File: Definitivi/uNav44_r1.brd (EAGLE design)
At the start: 39.6 x 39.6 mm, 37 parts, among them IC1 DSPIC33FJ128MC, IC2 24LC024, Q1 10MHz

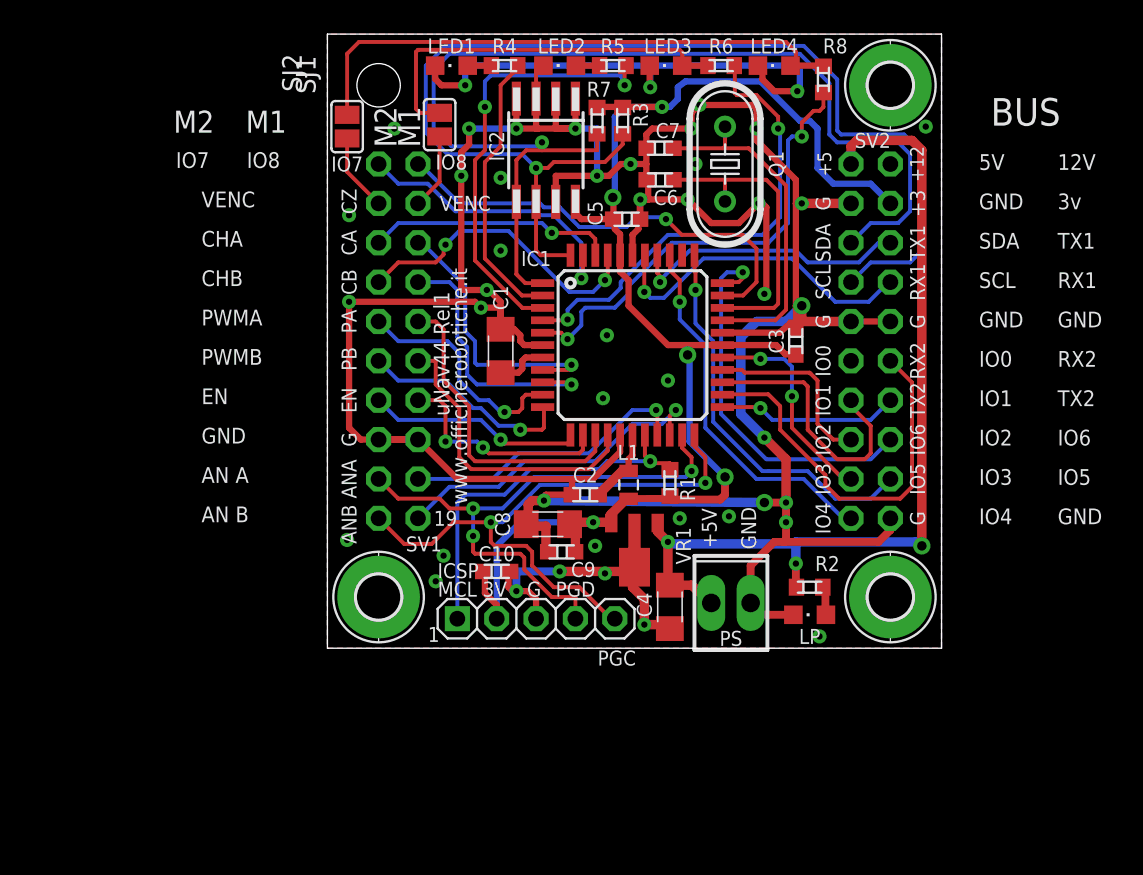
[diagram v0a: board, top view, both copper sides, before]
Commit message: Add Vencoder voltage selection \ Removed connection of LED3 and LED4 from connector \ @katodo : PCB update is needed
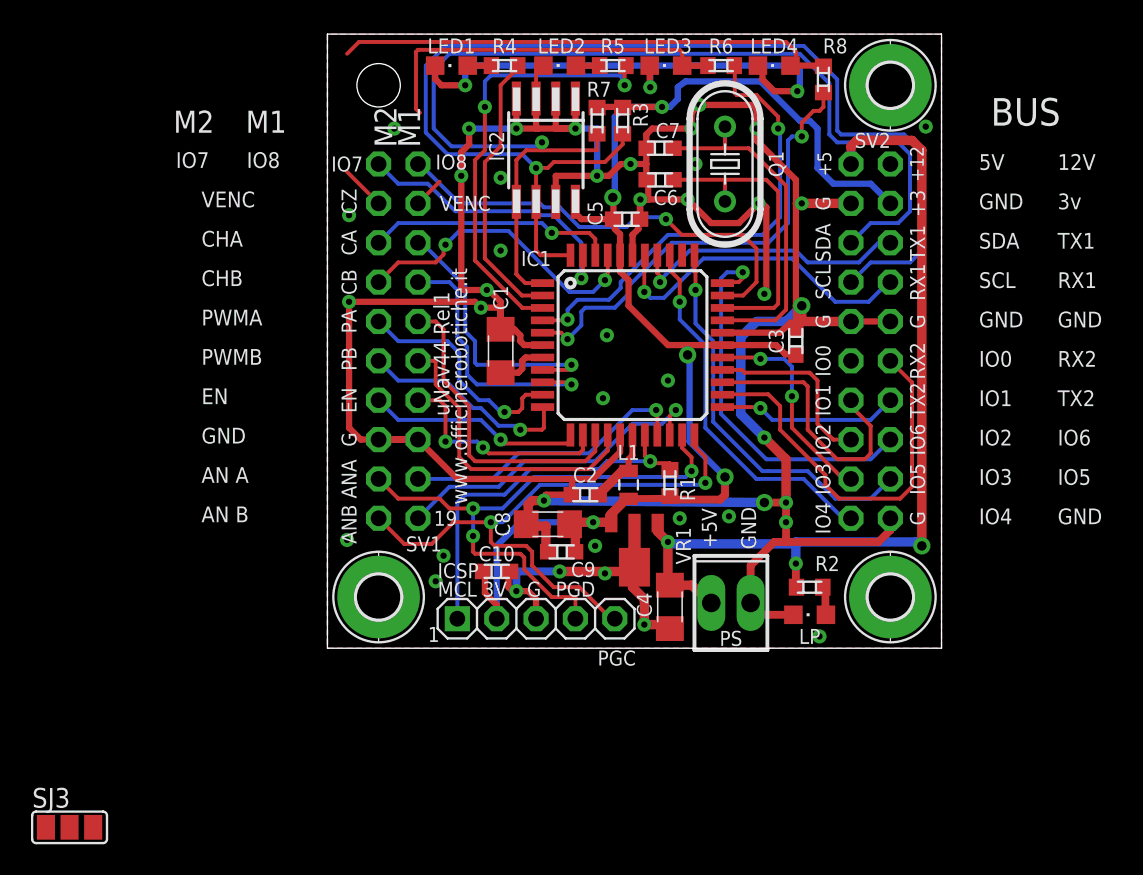
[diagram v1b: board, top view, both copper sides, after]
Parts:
- removed SJ1, SJ2: (no value), jumper:SJ
- added SJ3: (no value), jumper:SJ_2
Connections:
- removed net VENC1: SJ2.2, SV1.3
- removed net VENC2: SJ1.2, SV1.4
- new net VENC: SV1.3, SV1.4
- net +3V3: now also SJ3.1
- net +5V: now also SJ3.3
- net VENC1-LD3: no longer SJ2.1
- net VENC2-LD4: no longer SJ1.1
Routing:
- net VENC2: track 5.03 -> 0.00 mm
- net VENC1: track 4.90 -> 0.00 mm
- net VENC: track 0.00 -> 4.85 mm
- net VENC2-LD4: track 36.9 -> 33.0 mm
- net VENC1-LD3: track 25.1 -> 23.9 mm
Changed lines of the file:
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@@
 <element name="H2" library="holes" package="2,8-PAD" value="MOUNT-PAD-ROUND2.8" x="33.02" y="0" smashed="yes"/>
 <element name="H3" library="holes" package="2,8-PAD" value="MOUNT-PAD-ROUND2.8" x="33.02" y="33.02" smashed="yes"/>
-<element name="SJ1" library="jumper" package="SJ" value="" x="-2.032" y="30.353" smashed="yes" rot="R270">
-<attribute name="NAME" x="-5.334" y="34.925" size="1.27" layer="25" ratio="10" rot="R270"/>
-<attribute name="VALUE" x="-2.032" y="29.9529" size="0.02" layer="27" rot="R270"/>
-</element>
-<element name="SJ2" library="jumper" package="SJ" value="" x="3.937" y="30.48" smashed="yes" rot="R270">
-<attribute name="NAME" x="-6.223" y="35.052" size="1.27" layer="25" ratio="10" rot="R270"/>
-<attribute name="VALUE" x="3.937" y="30.0799" size="0.02" layer="27" rot="R270"/>
-</element>
+<element name="SJ3" library="jumper" package="SJ_2" value="" x="-19.939" y="-14.859"/>
 </elements>
 <signals>
@@
 <wire x1="5.207" y1="25.4" x2="2.667" y2="27.94" width="0.254" layer="16"/>
 <wire x1="2.54" y1="27.94" x2="2.667" y2="27.94" width="0.254" layer="16"/>
-</signal>
-<signal name="VENC1">
-<contactref element="SV1" pad="3"/>
-<contactref element="SJ2" pad="2"/>
-<wire x1="2.54" y1="25.4" x2="3.937" y2="26.797" width="0.254" layer="1"/>
-<wire x1="3.937" y1="26.797" x2="3.937" y2="29.718" width="0.254" layer="1"/>
 </signal>
 <signal name="CHA1">
@@
 <wire x1="34.671" y1="3.556" x2="26.924" y2="3.556" width="0.6096" layer="16"/>
 <wire x1="26.924" y1="3.556" x2="26.924" y2="3.429" width="0.6096" layer="16"/>
+<contactref element="SJ3" pad="3"/>
+<wire x1="18.669" y1="0.638" x2="-18.415" y2="-14.859" width="0" layer="19" extent="1-1"/>
 </signal>
 <signal name="+12V">
@@
 <wire x1="14.986" y1="4.826" x2="14.986" y2="4.799" width="0.6096" layer="1"/>
 <wire x1="14.986" y1="4.799" x2="15.01" y2="4.775" width="0.6096" layer="1"/>
+<contactref element="SJ3" pad="1"/>
+<wire x1="7.62" y1="-1.397" x2="-21.463" y2="-14.859" width="0" layer="19" extent="1-16"/>
 </signal>
 <signal name="GND">
@@
 <wire x1="28.829" y1="-1.143" x2="28.863" y2="-1.143" width="0.508" layer="1"/>
 </signal>
-<signal name="VENC2">
+<signal name="VENC">
 <contactref element="SV1" pad="4"/>
-<contactref element="SJ1" pad="2"/>
 <wire x1="0" y1="25.4" x2="-2.032" y2="27.432" width="0.254" layer="1"/>
-<wire x1="-2.032" y1="27.432" x2="-2.032" y2="29.591" width="0.254" layer="1"/>
+<contactref element="SV1" pad="3"/>
+<wire x1="2.54" y1="25.4" x2="3.937" y2="26.797" width="0.254" layer="1"/>
+<wire x1="0" y1="25.4" x2="2.54" y2="25.4" width="0" layer="19" extent="1-1"/>
 </signal>
 <signal name="VENC1-LD3">
 <contactref element="R6" pad="2"/>
 <contactref element="LED3" pad="A"/>
-<contactref element="SJ2" pad="1"/>
 <wire x1="21.248" y1="34.29" x2="19.592" y2="34.29" width="0.4064" layer="1"/>
 <wire x1="19.592" y1="34.29" x2="19.592" y2="35.145" width="0.254" layer="1"/>
@@
 <wire x1="2.413" y1="35.179" x2="2.413" y2="31.496" width="0.254" layer="1"/>
 <wire x1="2.413" y1="31.496" x2="2.667" y2="31.242" width="0.254" layer="1"/>
-<wire x1="2.667" y1="31.242" x2="3.937" y2="31.242" width="0.254" layer="1"/>
 </signal>
 <signal name="VENC2-LD4">
 <contactref element="R8" pad="2"/>
 <contactref element="LED4" pad="A"/>
-<contactref element="SJ1" pad="1"/>
 <wire x1="26.577" y1="34.29" x2="28.575" y2="34.29" width="0.4064" layer="1"/>
 <wire x1="28.575" y1="34.29" x2="28.702" y2="34.163" width="0.4064" layer="1"/>
 <wire x1="28.702" y1="34.163" x2="28.702" y2="34.251" width="0.4064" layer="1"/>
-<wire x1="-2.032" y1="31.115" x2="-2.032" y2="35.052" width="0.254" layer="1"/>
 <wire x1="-2.032" y1="35.052" x2="-1.27" y2="35.814" width="0.254" layer="1"/>
 <wire x1="-1.27" y1="35.814" x2="26.289" y2="35.814" width="0.254" layer="1"/>

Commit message: Add filter on ACS / Update with ACS filter and GND top layer / @katodo i suggest to check files
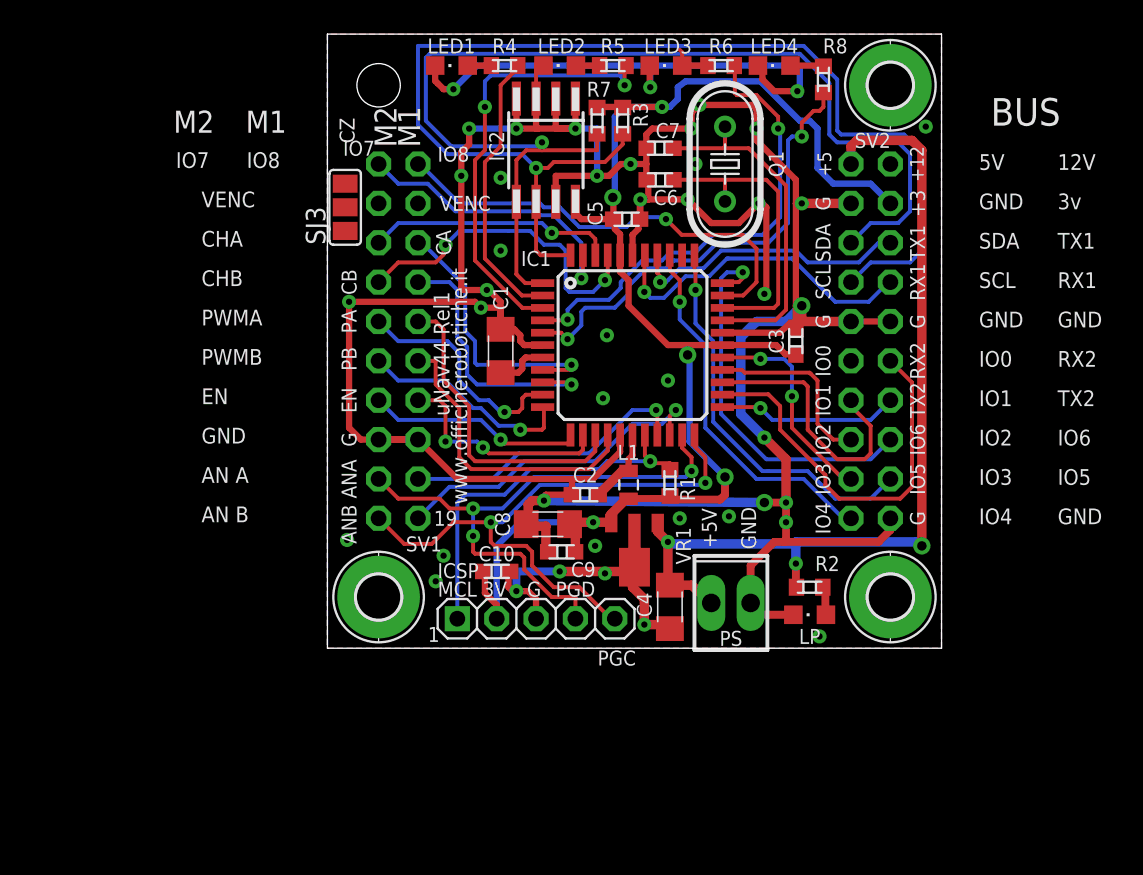
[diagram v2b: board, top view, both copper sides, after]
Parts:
- moved SJ3 43.8 mm to (-2.16, 25.1), turned to 90 degrees
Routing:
- net VENC2-LD4: track 33.0 -> 2.61 mm
- net VENC1-LD3: track 23.9 -> 2.74 mm
- net VENC: track 4.85 -> 0.00 mm
- net SCL: track 75.9 -> 77.4 mm
- net CHB2: track 19.9 -> 21.3 mm
- net SDA: track 71.8 -> 73.0 mm
- net GND: track 280.0 -> 279.7 mm, vias 46 -> 44
